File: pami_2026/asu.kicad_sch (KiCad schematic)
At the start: 11 parts, among them J2 Conn_01x03_Pin, J3 Conn_01x03_Pin, J4 Conn_01x03_Pin, SW1 SW_Reed

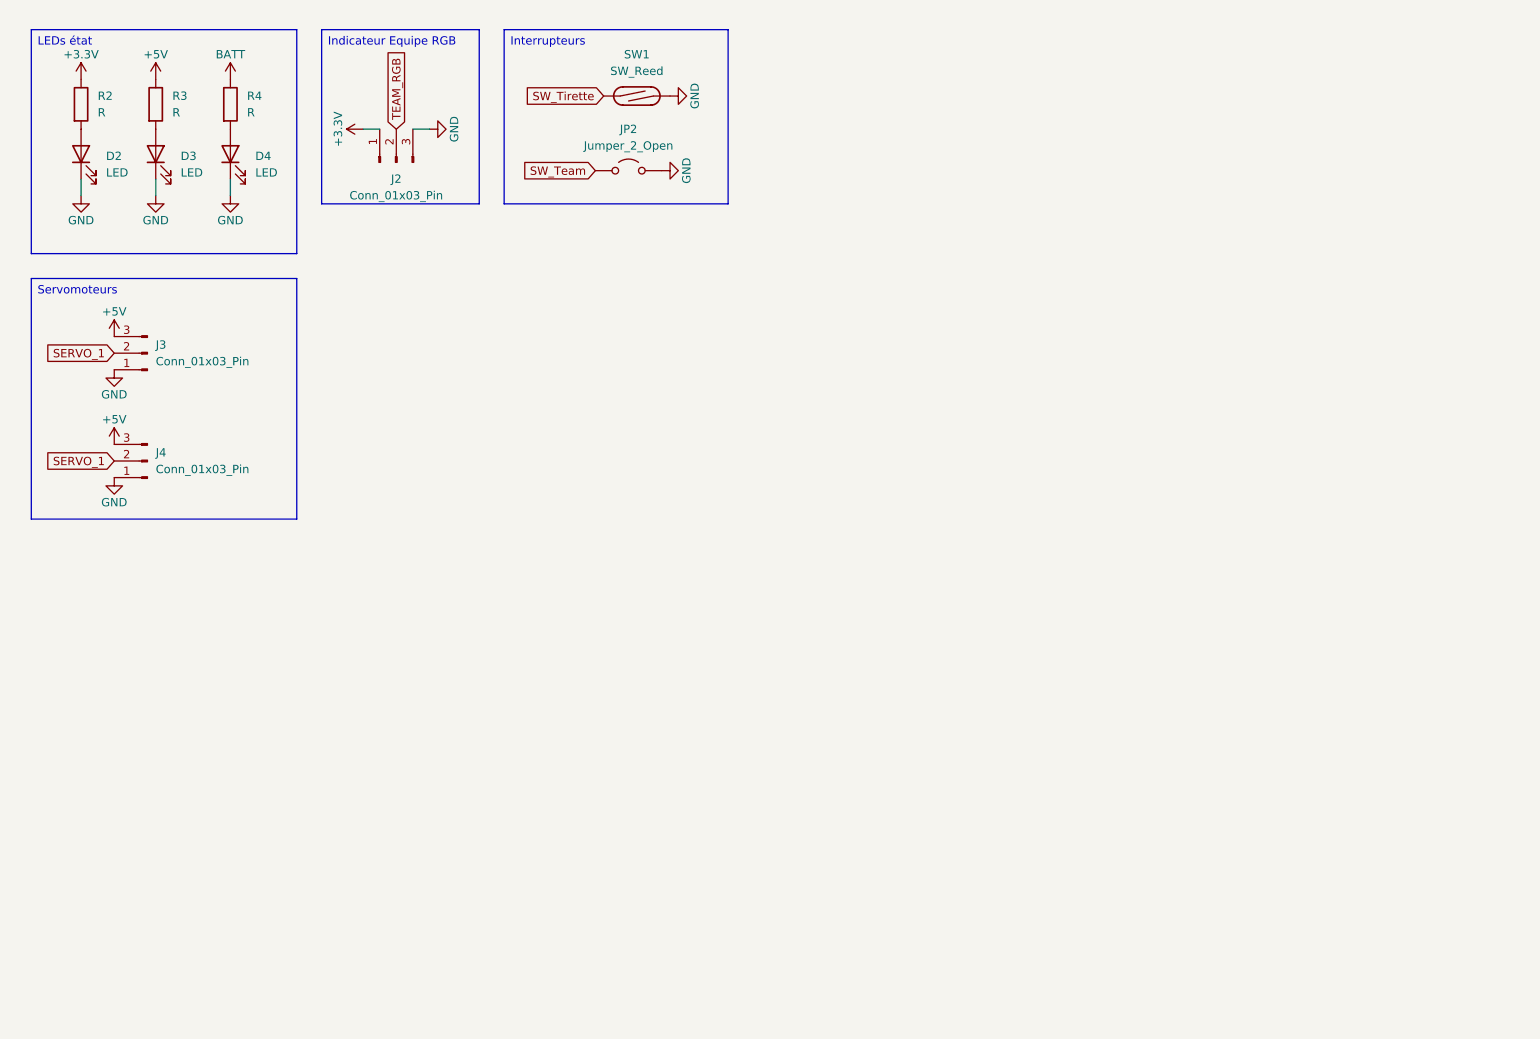
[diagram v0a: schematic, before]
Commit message: WIP USB programmer
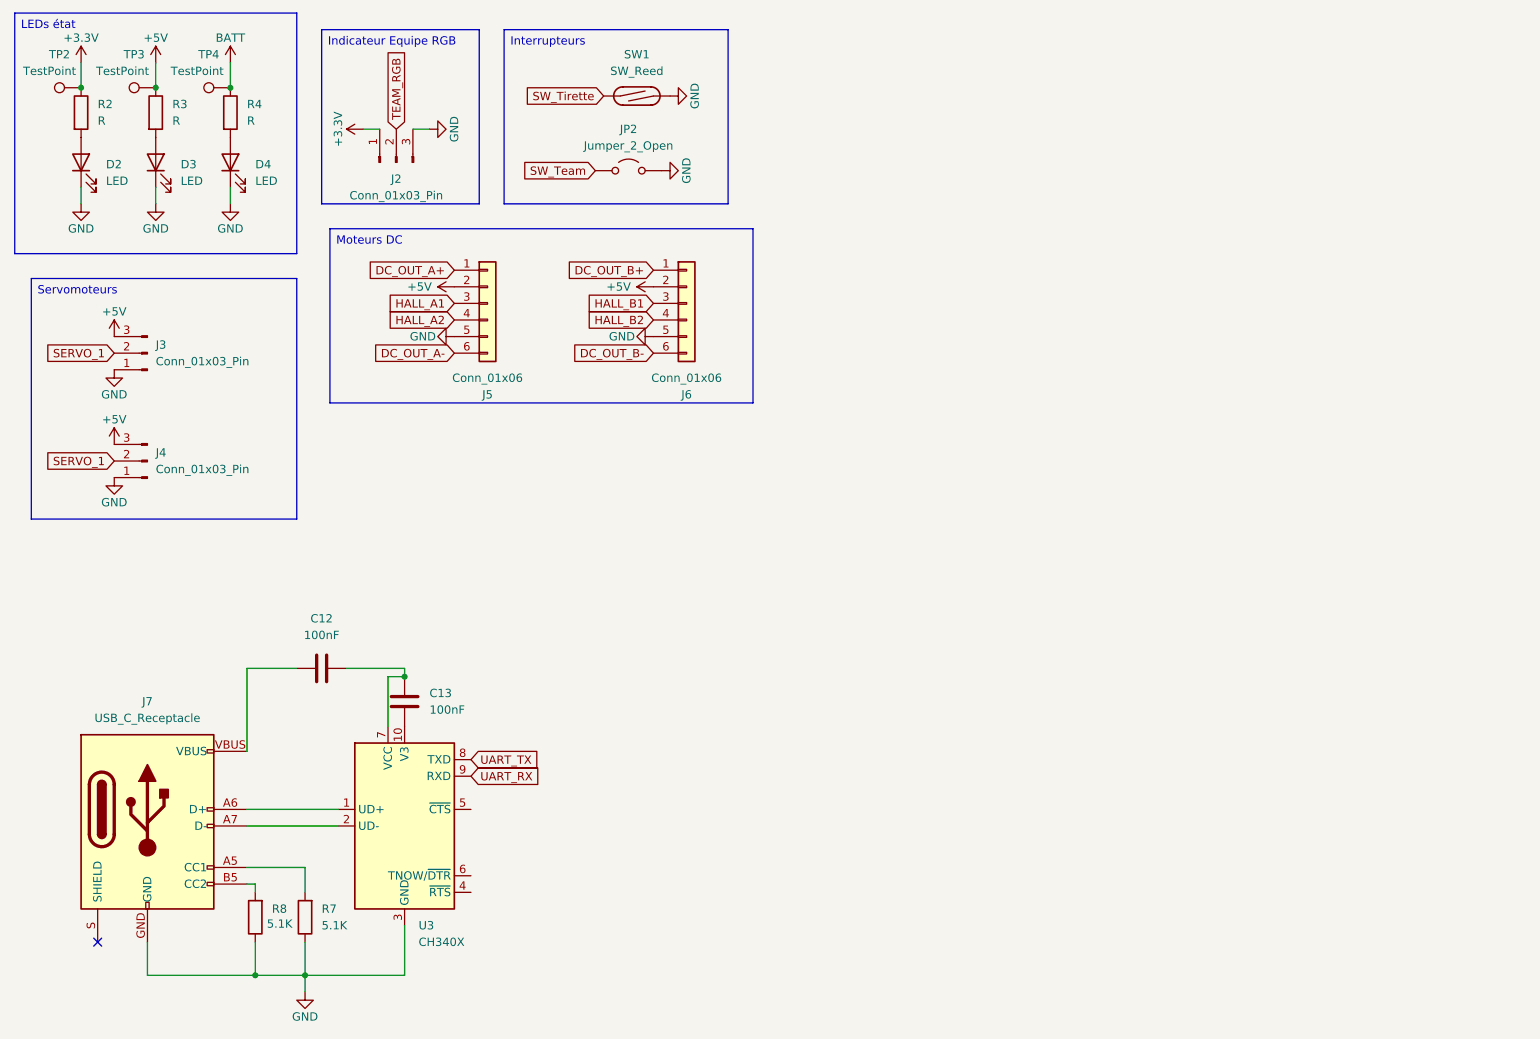
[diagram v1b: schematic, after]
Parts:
- added C12, C13: 100nF, symbol Device:C
- added J5, J6: Conn_01x06, PCM_SparkFun-Connector:1x06_P2.54mm_Socket_Vertical_SMD_Pin1RightDown, symbol PCM_SparkFun-Connector:Conn_01x06_P2.54mm_Socket_Vertical_SMD_Pin1RightDown
- added J7: USB_C_Receptacle, PCM_SparkFun-Connector:USB-C_16, symbol PCM_SparkFun-Connector:USB_C_Receptacle
- added R7, R8: 5.1K, symbol Device:R
- added TP2, TP3, TP4: TestPoint, symbol Connector:TestPoint
- added U3: CH340X, Package_SO:MSOP-10_3x3mm_P0.5mm, symbol Interface_USB:CH340X
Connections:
- net +3.3V: now also TP2.1
- net +5V: now also J5.2 (Pin_2), J6.2 (Pin_2), TP3.1
- net BATT: now also TP4.1
- net GND: now also J5.5 (Pin_5), J6.5 (Pin_5), J7.GND, R7.1, R8.1, U3.3 (GND)
- new net: J7.A5 (CC1), R7.2
- new net: J7.A6 (D+), J7.B6 (D+), U3.1 (UD+)
- new net: C13.2, U3.10 (V3)
- new net: J7.A7 (D-), J7.B7 (D-), U3.2 (UD-)
- new net: C12.2, C13.1, U3.7 (VCC)
- new net: J7.B5 (CC2), R8.2
- new net: C12.1, J7.VBUS
- new net DC_OUT_A+: J5.1 (Pin_1)
- new net DC_OUT_A-: J5.6 (Pin_6)
- new net DC_OUT_B+: J6.1 (Pin_1)
- new net DC_OUT_B-: J6.6 (Pin_6)
- new net HALL_A1: J5.3 (Pin_3)
- new net HALL_A2: J5.4 (Pin_4)
- new net HALL_B1: J6.3 (Pin_3)
- new net HALL_B2: J6.4 (Pin_4)
- new net UART_RX: U3.9 (RXD)
- new net UART_TX: U3.8 (TXD)
- no-connect marks 0 -> 1
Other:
- moved on the sheet: D2, D3, D4, R2, R3, R4

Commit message: Change DC drivers, apply datasheet recommendations, add big capacitor, remove USB programmer for simple connector
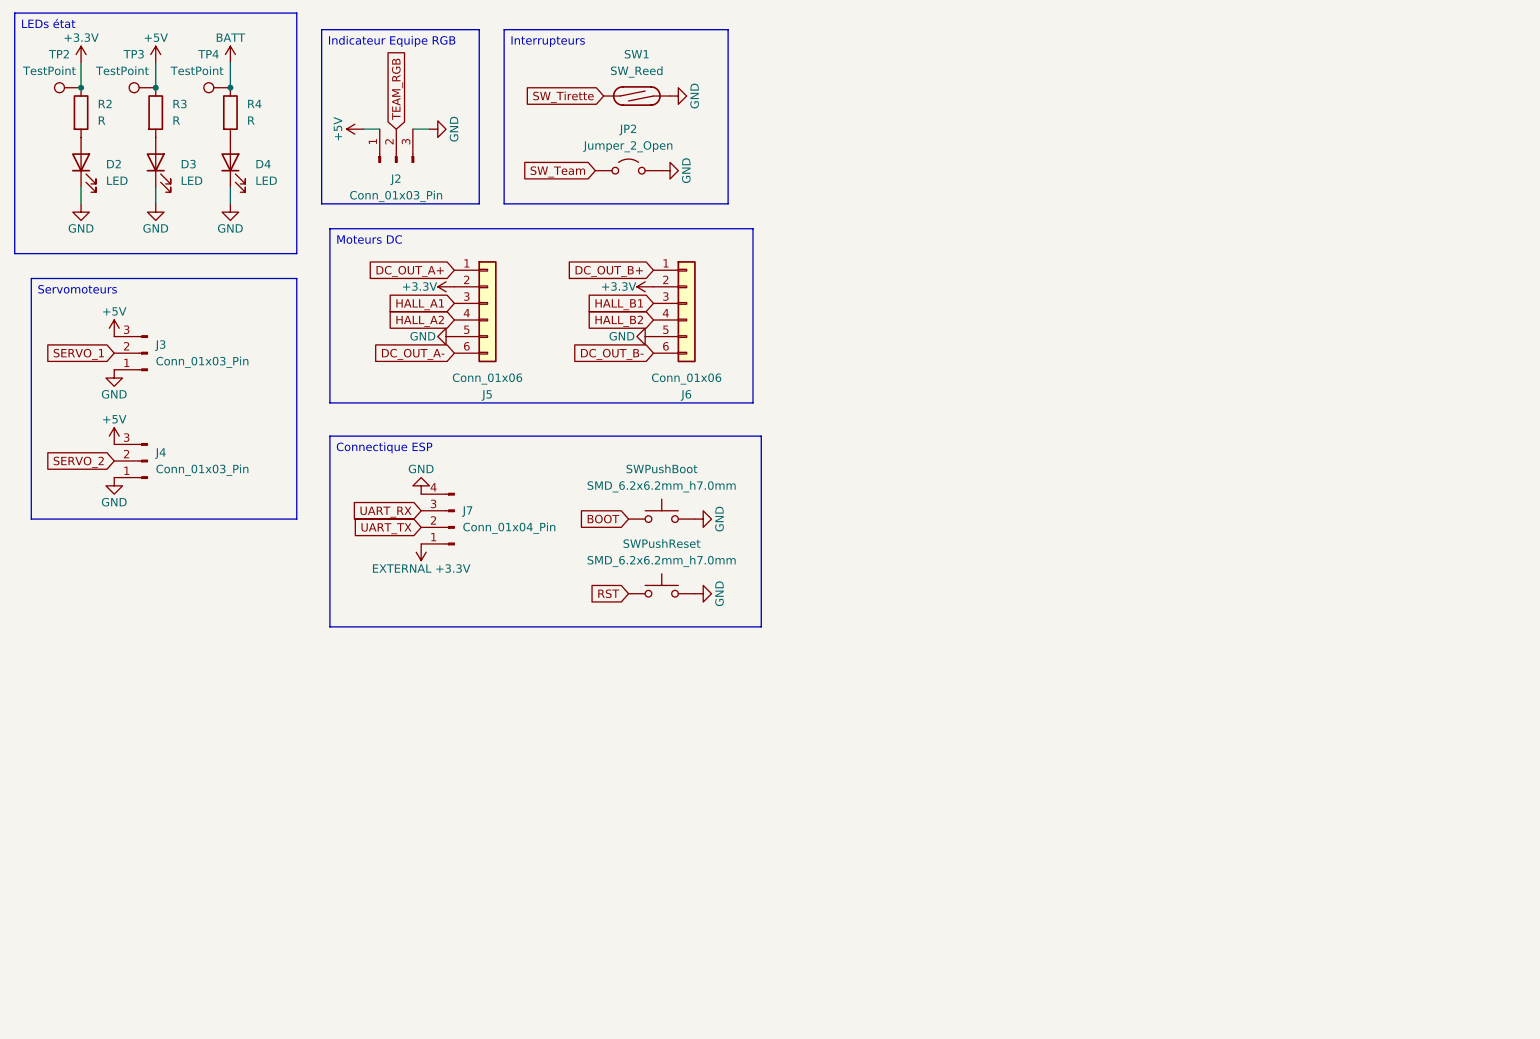
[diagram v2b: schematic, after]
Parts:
- removed C12, C13: 100nF, symbol Device:C
- removed J7: USB_C_Receptacle, PCM_SparkFun-Connector:USB-C_16, symbol PCM_SparkFun-Connector:USB_C_Receptacle
- removed R7, R8: 5.1K, symbol Device:R
- removed U3: CH340X, Package_SO:MSOP-10_3x3mm_P0.5mm, symbol Interface_USB:CH340X
- added J7: Conn_01x04_Pin, symbol Connector:Conn_01x04_Pin
- added SWPushBoot, SWPushReset: SMD_6.2x6.2mm_h7.0mm, PCM_SparkFun-Switch:Push_SMD_6.2x6.2mm, symbol PCM_SparkFun-Switch:SPST_Push_SMD_6.2x6.2mm_h7.0mm
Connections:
- net +3.3V: now also J5.2 (Pin_2), J6.2 (Pin_2); no longer J2.1 (Pin_1)
- net +5V: now also J2.1 (Pin_1); no longer J5.2 (Pin_2), J6.2 (Pin_2)
- net GND: now also J7.4 (Pin_4), SWPushBoot.2, SWPushReset.2
- net SERVO_1: no longer J4.2 (Pin_2)
- net UART_RX: now also J7.3 (Pin_3)
- net UART_TX: now also J7.2 (Pin_2)
- new net BOOT: SWPushBoot.1
- new net EXTERNAL +3.3V: J7.1 (Pin_1)
- new net RST: SWPushReset.1
- new net SERVO_2: J4.2 (Pin_2)
- no-connect marks 1 -> 0

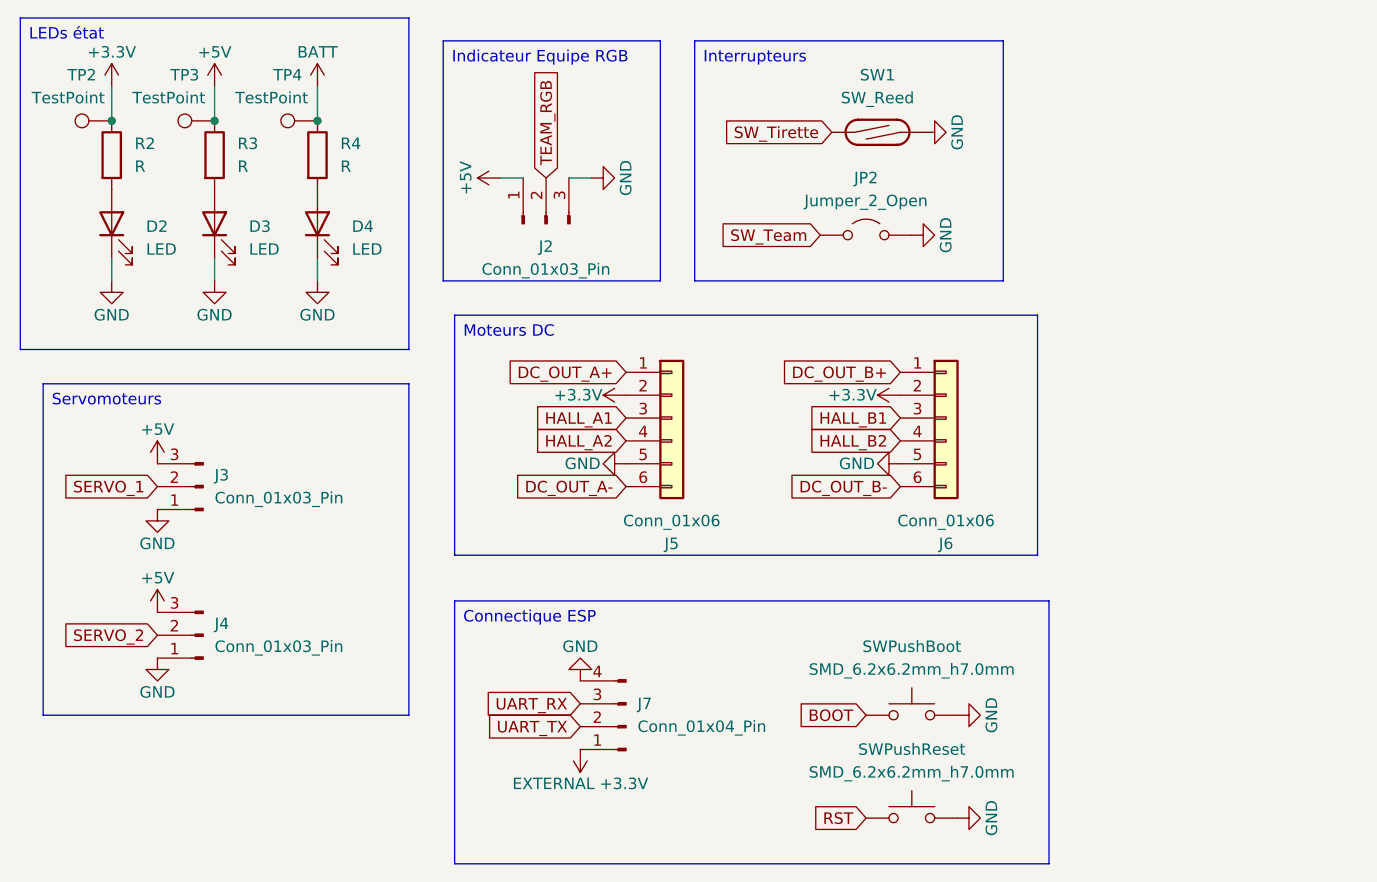
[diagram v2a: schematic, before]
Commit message: Ultrason, empreintes et petites corrections
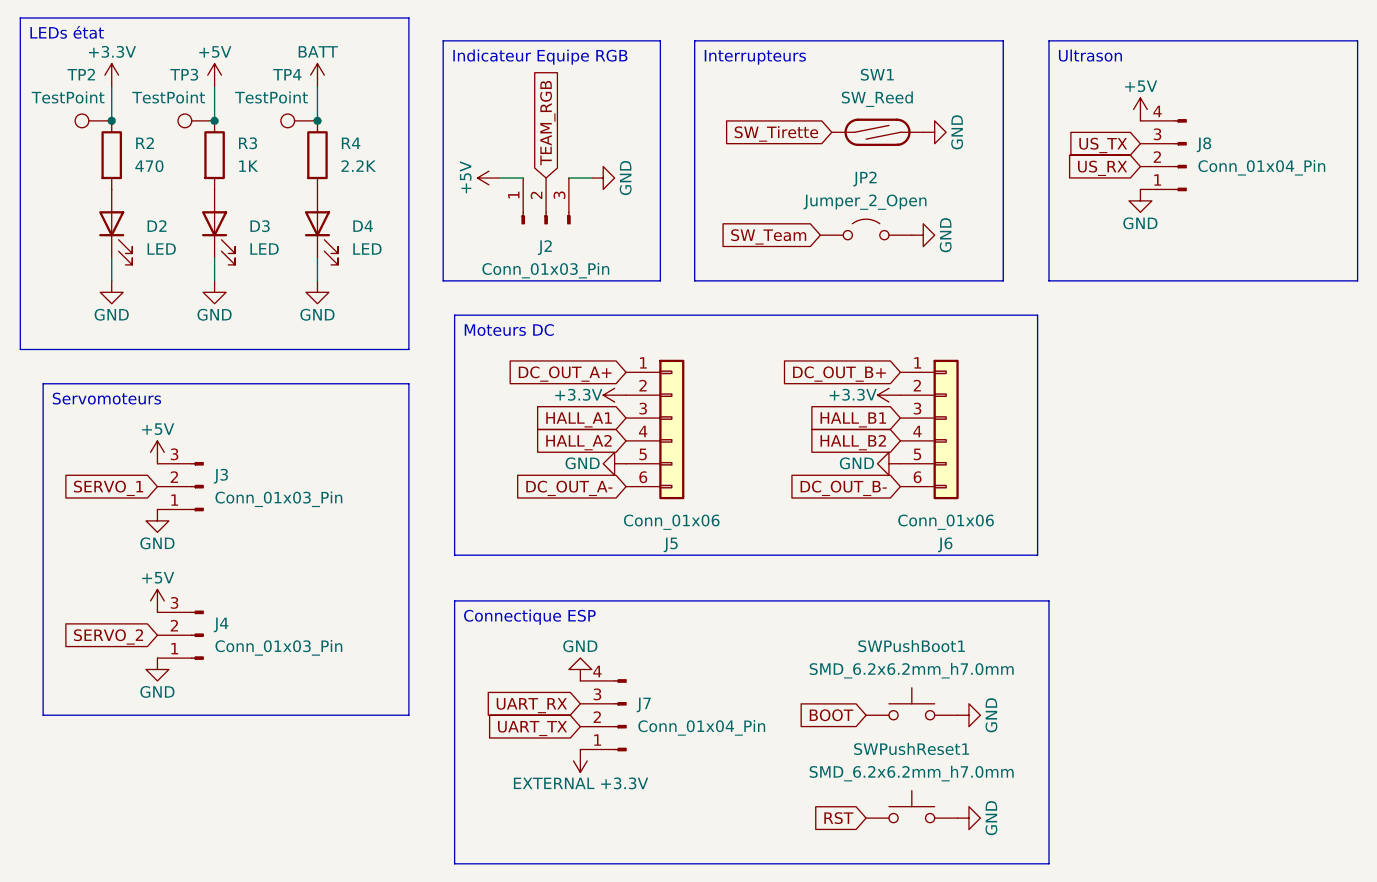
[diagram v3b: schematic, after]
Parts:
- added J8: Conn_01x04_Pin, Connector_PinHeader_2.54mm:PinHeader_1x04_P2.54mm_Vertical, symbol Connector:Conn_01x04_Pin
- D2, D3, D4: footprint PCM_SparkFun-LED:LED_0603_1608Metric -> LED_SMD:LED_0603_1608Metric
- J2, J3, J4: footprint (none) -> Connector_PinHeader_2.54mm:PinHeader_1x03_P2.54mm_Vertical
- J5, J6: footprint PCM_SparkFun-Connector:1x06_P2.54mm_Socket_Vertical_SMD_Pin1RightDown -> Connector_PinHeader_2.54mm:PinHeader_1x06_P2.54mm_Vertical
- J7: footprint (none) -> Connector_PinHeader_2.54mm:PinHeader_1x04_P2.54mm_Vertical
- JP2: footprint (none) -> Jumper:SolderJumper-2_P1.3mm_Open_RoundedPad1.0x1.5mm
- R2: value R -> 470; footprint PCM_SparkFun-Resistor:R_0603_1608Metric -> Resistor_SMD:R_0603_1608Metric
- R3: value R -> 1K; footprint PCM_SparkFun-Resistor:R_0603_1608Metric -> Resistor_SMD:R_0603_1608Metric
- R4: value R -> 2.2K; footprint PCM_SparkFun-Resistor:R_0603_1608Metric -> Resistor_SMD:R_0603_1608Metric
- SW1: footprint (none) -> Connector_PinHeader_2.54mm:PinHeader_1x02_P2.54mm_Vertical
- TP2, TP3, TP4: footprint (none) -> TestPoint:TestPoint_Pad_1.0x1.0mm
- renumbered SWPushBoot to SWPushBoot1, SWPushReset to SWPushReset1
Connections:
- net +5V: now also J8.4 (Pin_4)
- net GND: now also J8.1 (Pin_1)
- new net US_RX: J8.2 (Pin_2)
- new net US_TX: J8.3 (Pin_3)

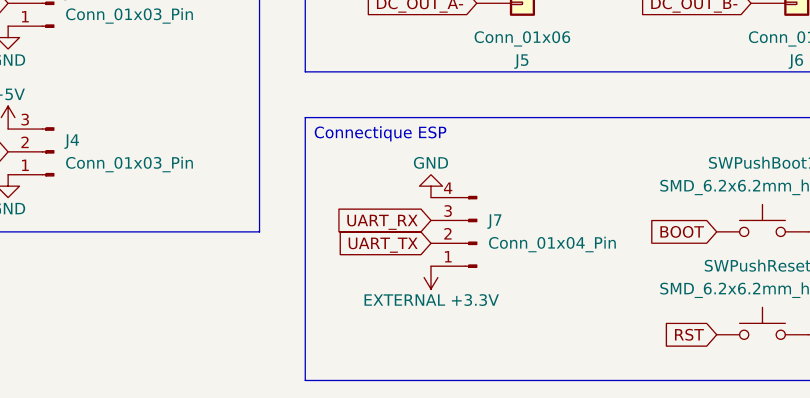
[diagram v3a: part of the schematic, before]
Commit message: Fix: ERC is Happy - proper footprints - Feat: add multiplexer for external power
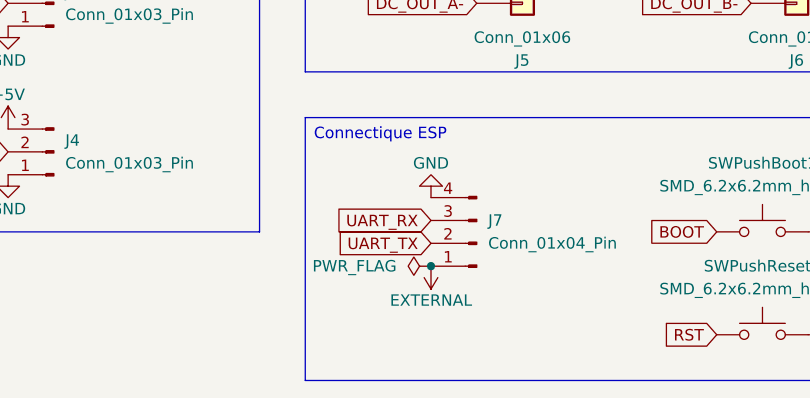
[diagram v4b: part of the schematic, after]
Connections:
- net EXTERNAL +3.3V renamed EXTERNAL
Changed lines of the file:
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@@
+		(color 0 0 0 0)
+	)
+	(junction
+		(at 80.01 95.25)
+		(diameter 0)
 		(color 0 0 0 0)
 	)
@@
 			)
 		)
-		(property "Value" "EXTERNAL +3.3V"
+		(property "Value" "EXTERNAL"
 			(at 80.01 99.06 0)
 			(do_not_autoplace yes)
@@
 					(unit 1)
 				)
+			)
+		)
+	)
+	(symbol
+		(lib_id "power:PWR_FLAG")
+		(at 80.01 95.25 90)
+		(unit 1)
+		(exclude_from_sim no)
+		(in_bom yes)
+		(on_board yes)
+		(dnp no)
+		(fields_autoplaced yes)
+		(property "Reference" "#FLG05"
+			(at 78.105 95.25 0)
+			(effects
+				(font
+					(size 1.27 1.27)
+				)
+				(hide yes)
+			)
+		)
+		(property "Value" "PWR_FLAG"
+			(at 76.2 95.2499 90)
+			(effects
+				(font
+					(size 1.27 1.27)
+				)
+				(justify left)
+			)
+		)
+		(property "Footprint" ""
+			(at 80.01 95.25 0)
+			(effects
+				(font
+					(size 1.27 1.27)
+				)
+				(hide yes)
+			)
+		)
+		(property "Datasheet" "~"
+			(at 80.01 95.25 0)
+			(effects
+				(font
+					(size 1.27 1.27)
+				)
+				(hide yes)
+			)
+		)
+		(property "Description" "Special symbol for telling ERC where power comes from"
+			(at 80.01 95.25 0)
+			(effects
+				(font
+					(size 1.27 1.27)
+				)
+				(hide yes)
+			)
+		)
+		(pin "1"
+		)
+		(instances
+			(project ""
+				(path "/2e16a05b-e8ca-4fff-9c3e-5c880745daa6/bb7fbca0-80fe-418e-a09d-cb4c86ee0cfe"
+					(reference "#FLG05")
+					(unit 1)
+				)

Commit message: FEAT : Routing
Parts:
- removed JP2: Jumper_2_Open, Jumper:SolderJumper-2_P1.3mm_Open_RoundedPad1.0x1.5mm, symbol Jumper:Jumper_2_Open
- added D6: LED, LED_SMD:LED_0603_1608Metric, symbol Device:LED
- added J10: Conn_01x02_Pin, Connector_PinHeader_2.54mm:PinHeader_1x02_P2.54mm_Vertical, symbol Connector:Conn_01x02_Pin
- added R21: 1K, Resistor_SMD:R_0603_1608Metric, symbol Device:R
- added TP1: TestPoint, TestPoint:TestPoint_Pad_1.0x1.0mm, symbol Connector:TestPoint
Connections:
- net GND: now also D6.1 (K), J10.1 (Pin_1)
- net SW_Team: now also J10.2 (Pin_2)
- new net: D6.2 (A), R21.2
- new net STATUS_ESP: R21.1, TP1.1
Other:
- moved on the sheet: D2, D3, D4, J2, J3, J4, J5, J6, J7, J8, R2, R3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
